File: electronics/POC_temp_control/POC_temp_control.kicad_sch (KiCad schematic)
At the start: 155 parts, among them J1 Conn_01x02, J2 Conn_01x07, J3 Conn_01x05, J4 Conn_01x06, J5 Conn_01x02, J6 Conn_01x02, Q1 PXT8050, Q2 PXT8050, Q3 PXT8550, Q4 Q_PMOS_DUAL, Q5 BC858B, Q6 BC847A, T1 10P_1P_2S, U1 SY8120, U2 MCP1702T-3302, U4 LM358, U5 OP07, U6 OP07, U7 OP07, U8 74XX4051, U9 74XX4051

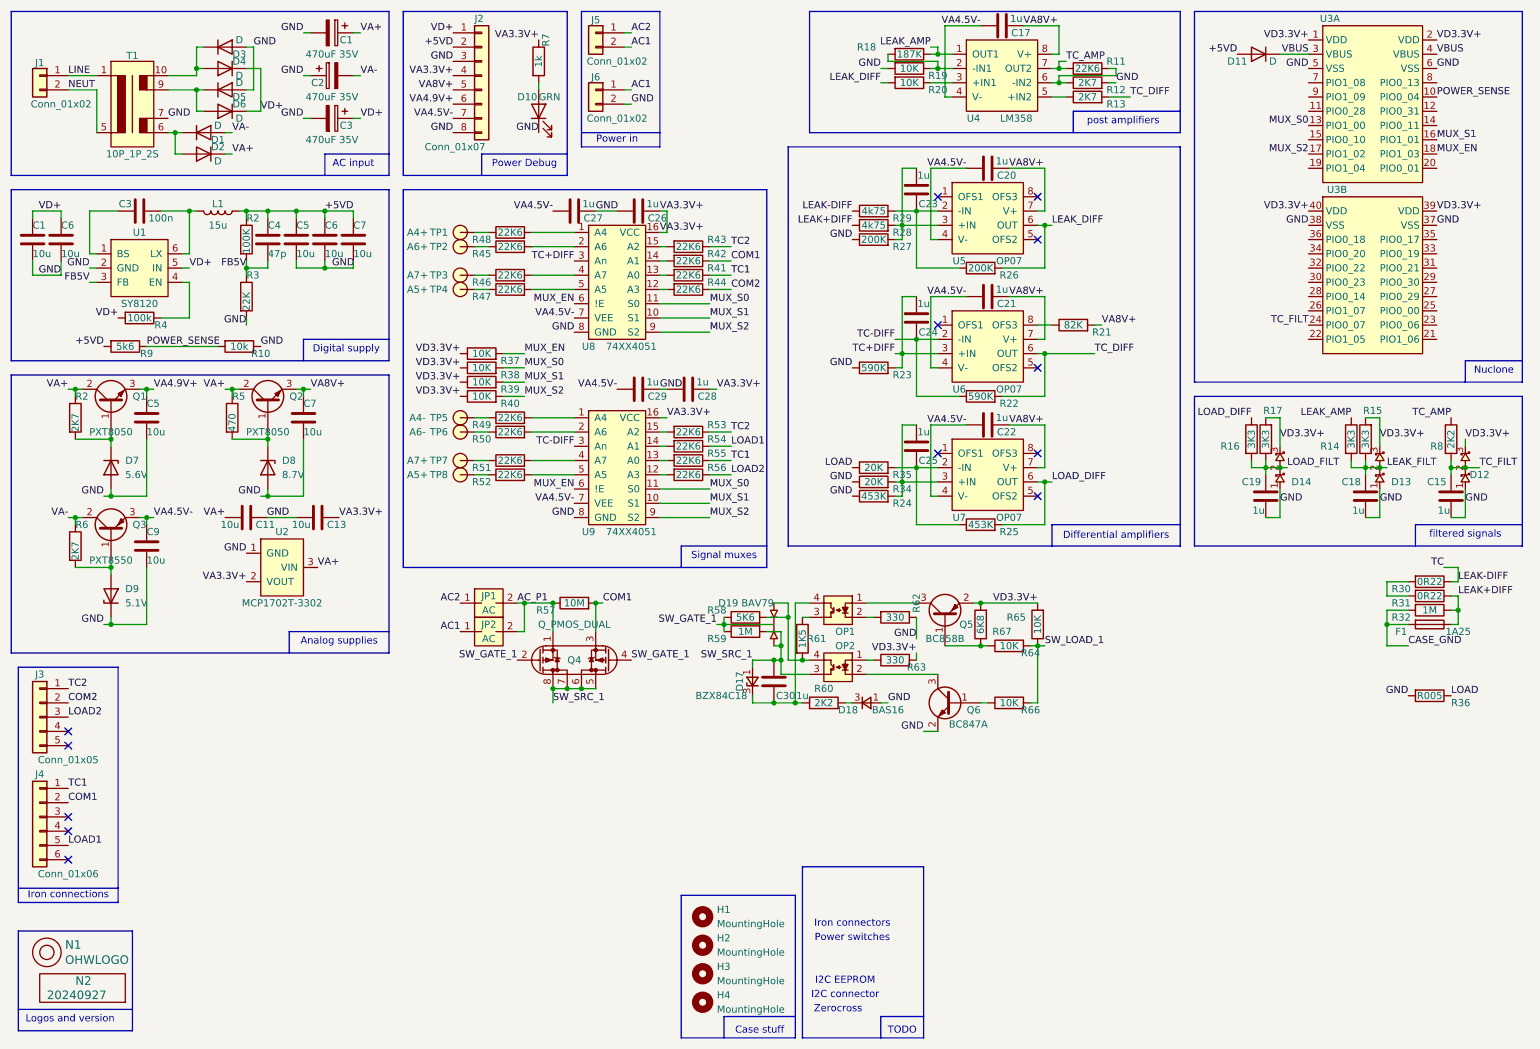
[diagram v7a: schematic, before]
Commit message: placed, duplicated power stage
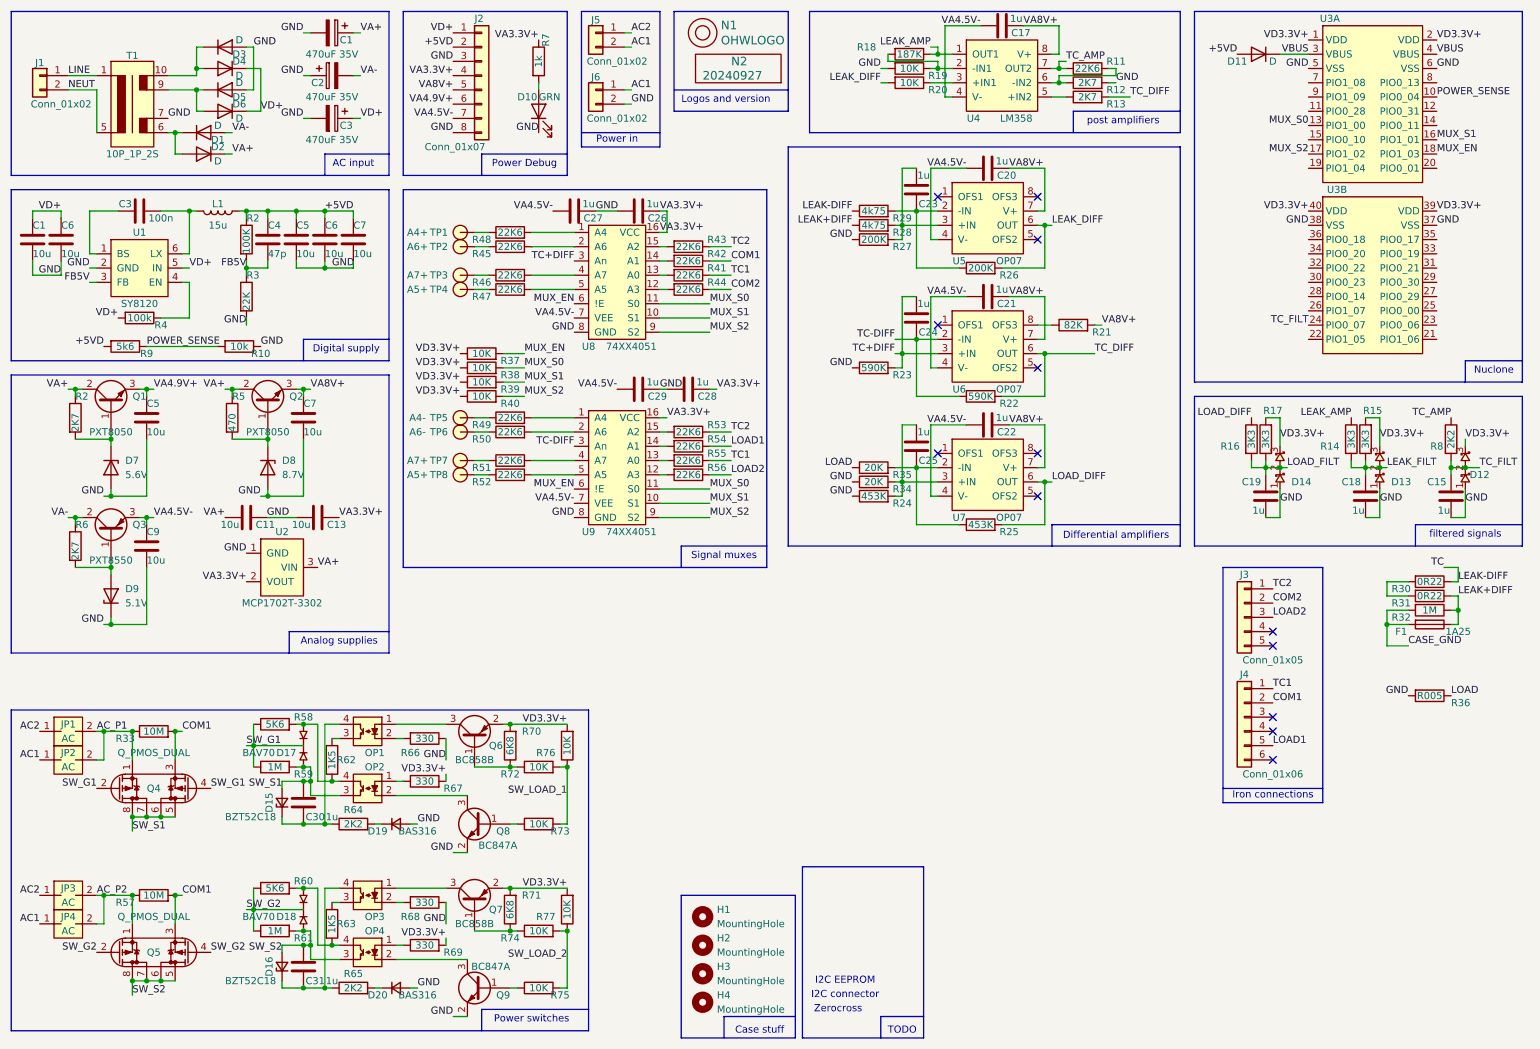
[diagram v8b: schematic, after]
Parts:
- removed D17: BZX84C18, SquantorIC:SOT23-3, symbol SquantorDevice:D_Zener_Small_A1C3
- removed D18: BAS16, SquantorIC:SOT23-3, symbol SquantorDevice:D_Small_A1C3
- removed D19: BAV79, SquantorIC:SOT23-3, symbol SquantorDevice:D_CC_AAC
- removed Q5: BC858B, SquantorIC:SOT23-3, symbol Device:Q_PNP_BEC
- removed Q6: BC847A, SquantorIC:SOT23-3, symbol Device:Q_NPN_BEC
- added C31: 1u, SquantorCapacitor:C_0805+0603, symbol Device:C
- added D15, D16: BZT52C18, SquantorDiodes:SOD-323-nexperia-hand, symbol SquantorDevice:D_Zener_Small_A2C1
- added D17, D18: BAV70, SquantorIC:SOT23-3, symbol SquantorDevice:D_CC_AAC
- added D19, D20: BAS316, SquantorDiodes:SOD-323-nexperia-hand, symbol SquantorDevice:D_Small_A2C1
- added JP3, JP4: AC, SquantorSpecial:solder_jumper_3mm_SMD, symbol SquantorSpecial:Solderjumper_2way_noconn
- added OP3, OP4: ~, SquantorOpto:OP_SOIC_4, symbol SquantorOpto:OP_Q_single
- added Q5: Q_PMOS_DUAL, SquantorIC:SOIC-8, symbol SquantorDevice:Q_PMOS_DUAL_8pin
- added Q6, Q7: BC858B, SquantorIC:SOT23-3, symbol Device:Q_PNP_BEC
- added Q8, Q9: BC847A, SquantorIC:SOT23-3, symbol Device:Q_NPN_BEC
- added R33: 10M, SquantorResistor:R_0603_hand, symbol Device:R
- added R68, R69: 330, SquantorResistor:R_0603_hand, symbol Device:R
- added R70, R71: 6K8, SquantorResistor:R_0603_hand, symbol Device:R
- added R72, R73, R74, R75, R76, R77: 10K, SquantorResistor:R_0603_hand, symbol Device:R
- R60: value 2K2 -> 5K6
- R61: value 1K5 -> 1M
- R62, R63: value 330 -> 1K5
- R64, R65: value 10K -> 2K2
- R66: value 10K -> 330
- R67: value 6K8 -> 330
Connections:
- net AC1: now also JP4.1
- net AC2: now also JP3.1
- net AC_P1: now also R33.1; no longer R57.1
- net COM1: now also Q5.3 (S2), R33.2
- net GND: now also R66.1, D19.2 (A), D20.2 (A), Q8.2 (E), Q9.2 (E), R68.1; no longer R62.1
- net SW_LOAD_1: now also R72.2, R73.2, R76.1; no longer R64.2, R65.1, R66.2
- net VD3.3V+: now also Q6.2 (E), Q7.2 (E), R69.2, R70.2, R71.2, R76.2, R77.2; no longer R63.2, R65.2
- net at R63.1: now also OP3.3; no longer OP2.1
- net at OP2.2: now also Q8.3 (C)
- net at OP2.4, R58.2: now also R62.2, D17.2 (K2); no longer R61.2
- net at C30.1, OP1.4: now also R64.1, D15.1 (K); no longer R60.1
- net at R60.2: now also R63.2, D18.2 (K2), OP4.4
- net at R67.1: now also OP2.1; no longer R64.1
- net at OP1.1: now also Q6.3 (C)
- net at OP1.3: now also R62.1; no longer R61.1
- net at OP1.2: now also R66.2; no longer R62.2
- net SW_GATE_1 renamed SW_G1
- net SW_G1: now also D17.3 (K1A2)
- net SW_SRC_1 renamed SW_S1
- net SW_S1: now also D15.2 (A), D17.1 (A1)
- new net: Q8.1 (B), R73.1
- new net: OP4.1, R69.1
- new net: Q6.1 (B), R70.1, R72.1
- new net: C31.1, D16.1 (K), OP3.4, R65.1
- new net: D20.1 (K), R65.2
- new net: OP4.2, Q9.3 (C)
- new net: OP3.1, Q7.3 (C)
- new net: OP3.2, R68.2
- new net: Q7.1 (B), R71.1, R74.1
- new net: D19.1 (K), R64.2
- new net: Q9.1 (B), R75.1
- new net AC_P2: JP3.2, JP4.2, Q5.1 (S1), R57.1
- new net SW_G2: D18.3 (K1A2), Q5.2 (G1), Q5.4 (G2), R60.1, R61.1
- new net SW_LOAD_2: R74.2, R75.2, R77.1
- new net SW_S2: C31.2, D16.2 (A), D18.1 (A1), OP4.3, Q5.5 (D2), Q5.6 (D2), Q5.7 (D1), Q5.8 (D1), R61.2
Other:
- note removed: "Iron connectors"
- moved on the sheet: J3, J4, N1, N2
